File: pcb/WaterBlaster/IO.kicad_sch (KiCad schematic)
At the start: 26 parts, among them J10 Conn_01x02, J11 Conn_01x02, J7 Conn_01x02, J8 Conn_01x02, J9 Conn_01x02

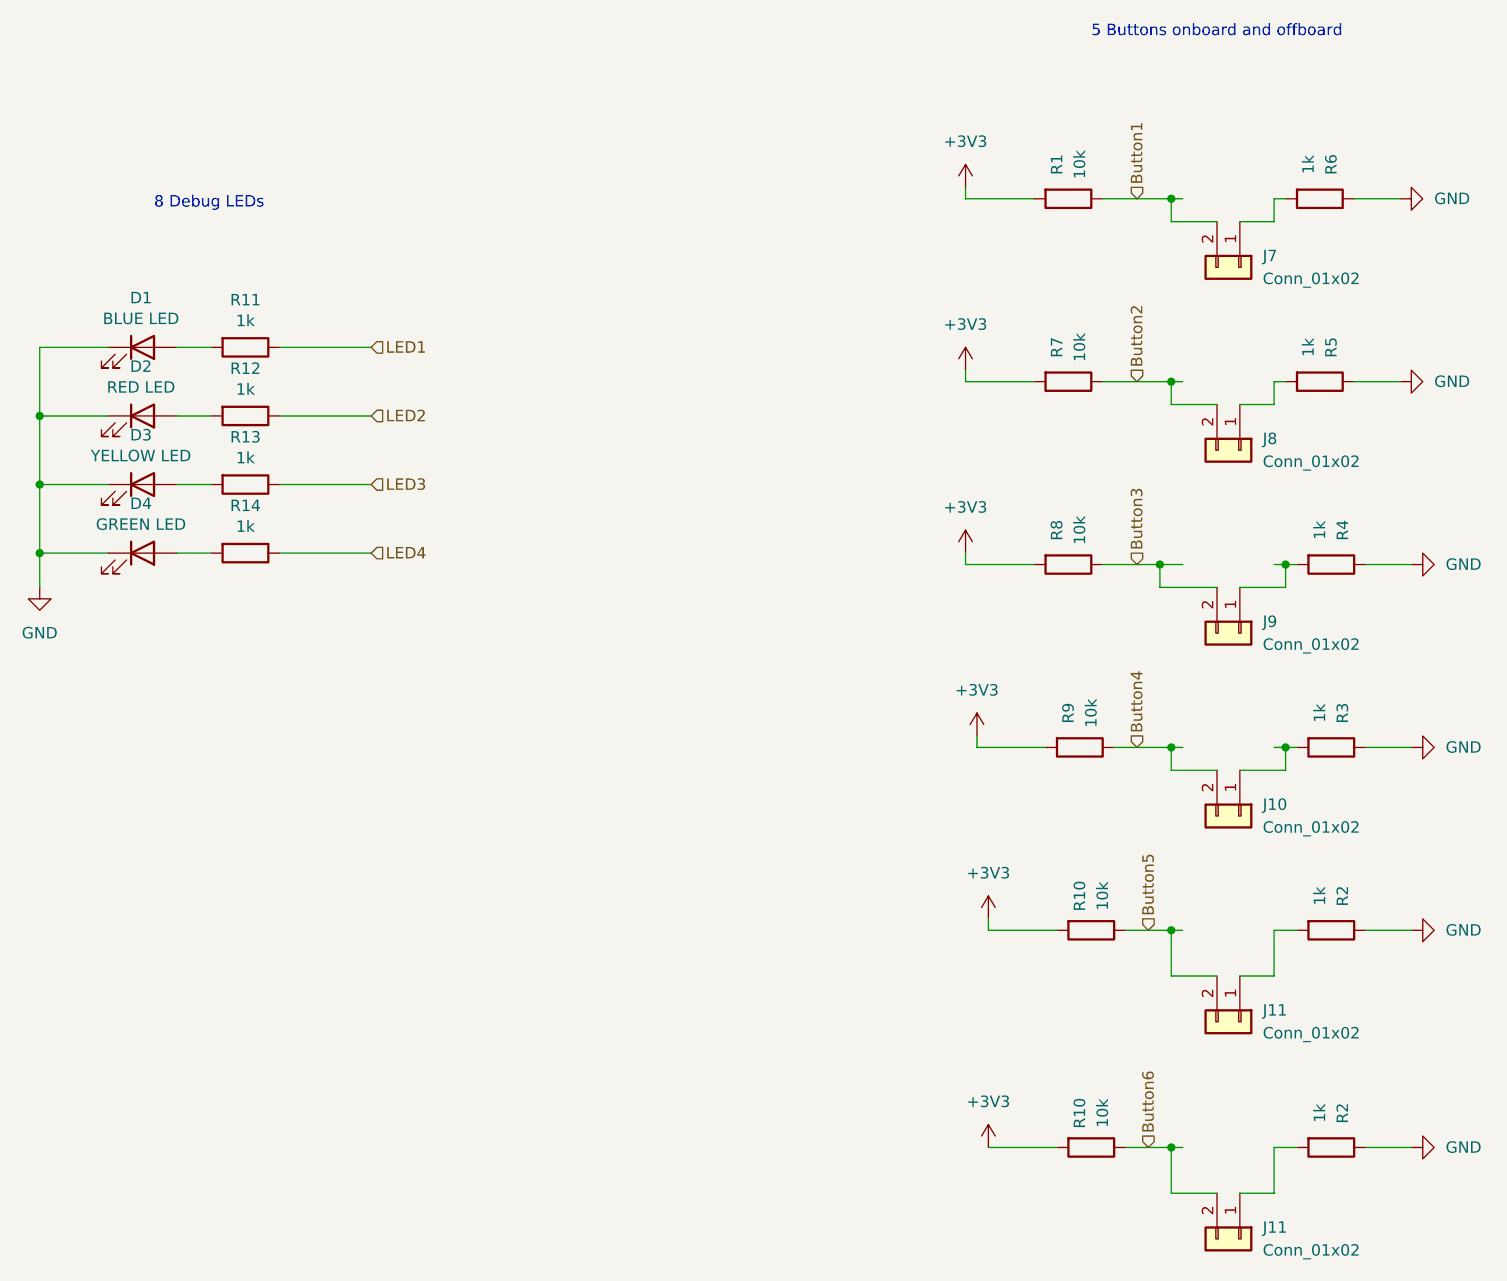
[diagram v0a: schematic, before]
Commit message: Updating firmware and CAD
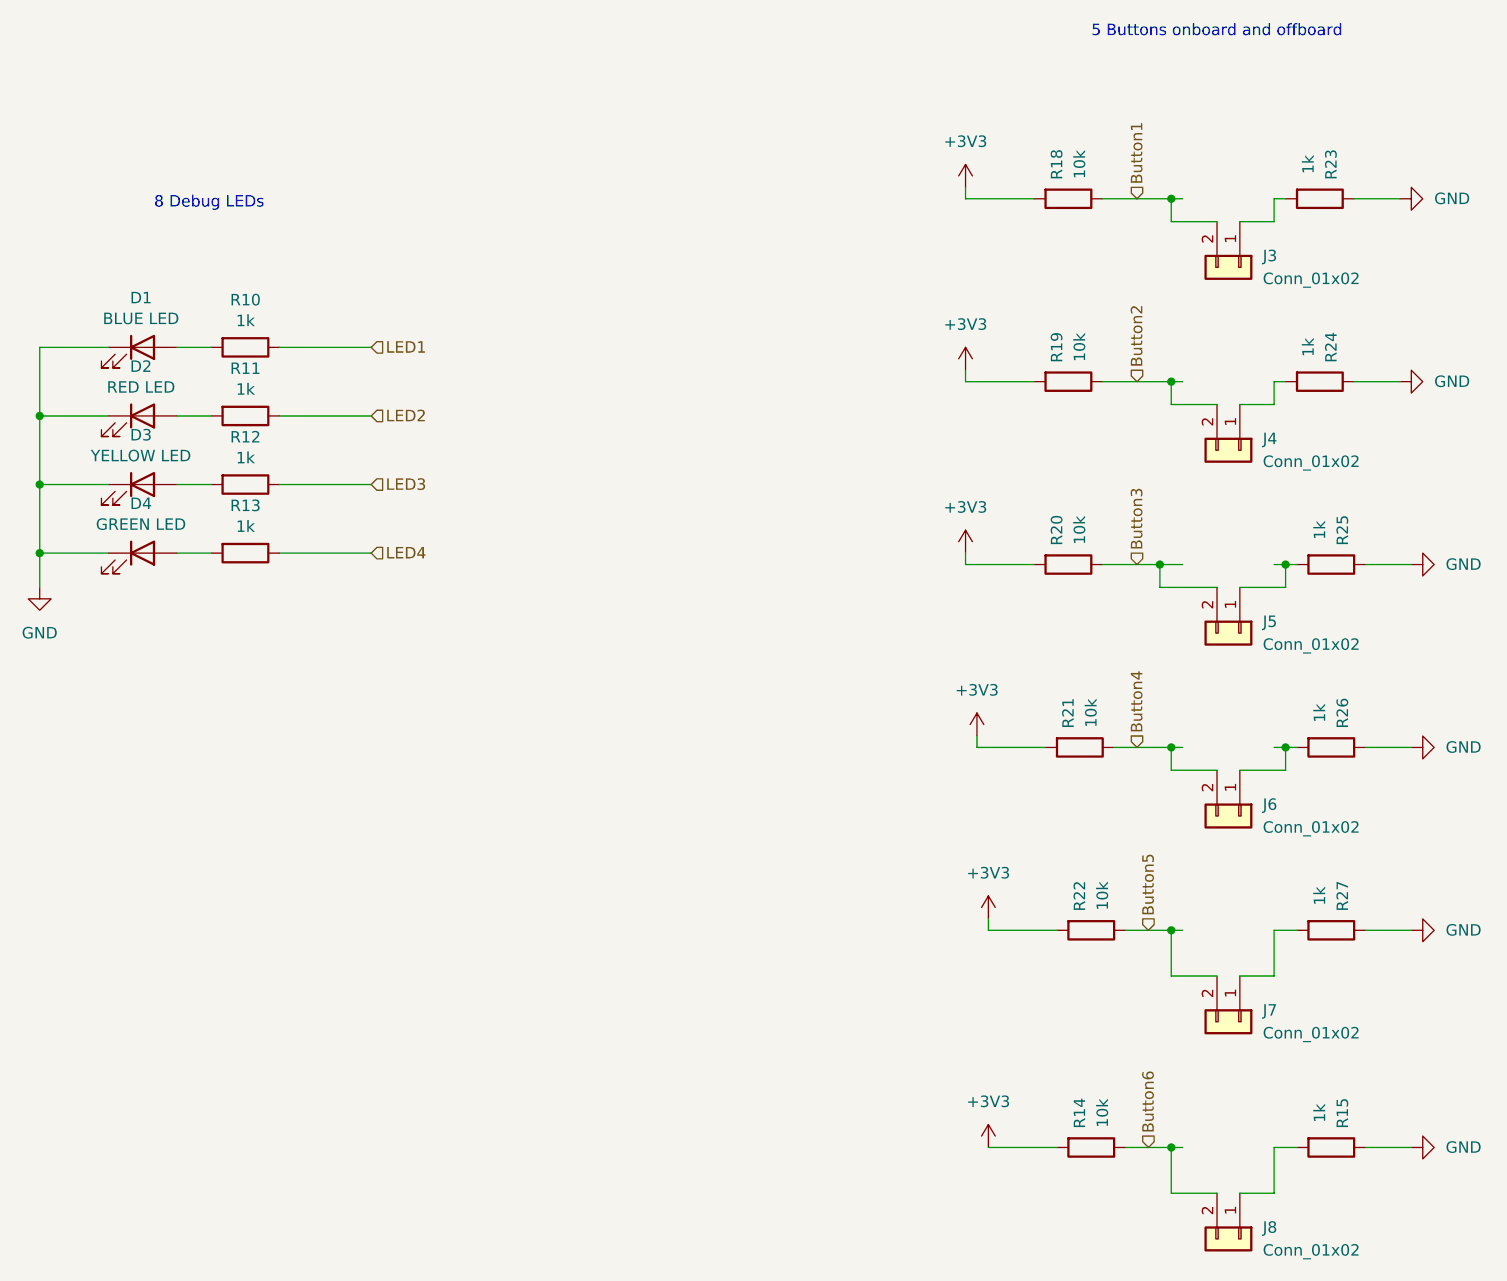
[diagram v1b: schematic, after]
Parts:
- renumbered J7 to J3, J8 to J4, J9 to J5, J10 to J6, J11 to J7, J11 to J8, R11 to R10, R12 to R11, R13 to R12, R14 to R13, R10 to R14, R2 to R15, R1 to R18, R7 to R19, R8 to R20, R9 to R21, R10 to R22, R6 to R23, R5 to R24, R4 to R25, R3 to R26, R2 to R27
